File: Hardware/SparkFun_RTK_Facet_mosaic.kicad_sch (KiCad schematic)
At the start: 29 parts, among them J3 Qwiic_RA, J5 Conn_01x12_FPC_0.5mm, J6 Conn_01x12_FPC_0.5mm, J7 Conn_01x12_FPC_0.5mm, U1 ESP32-PICO-V3-02

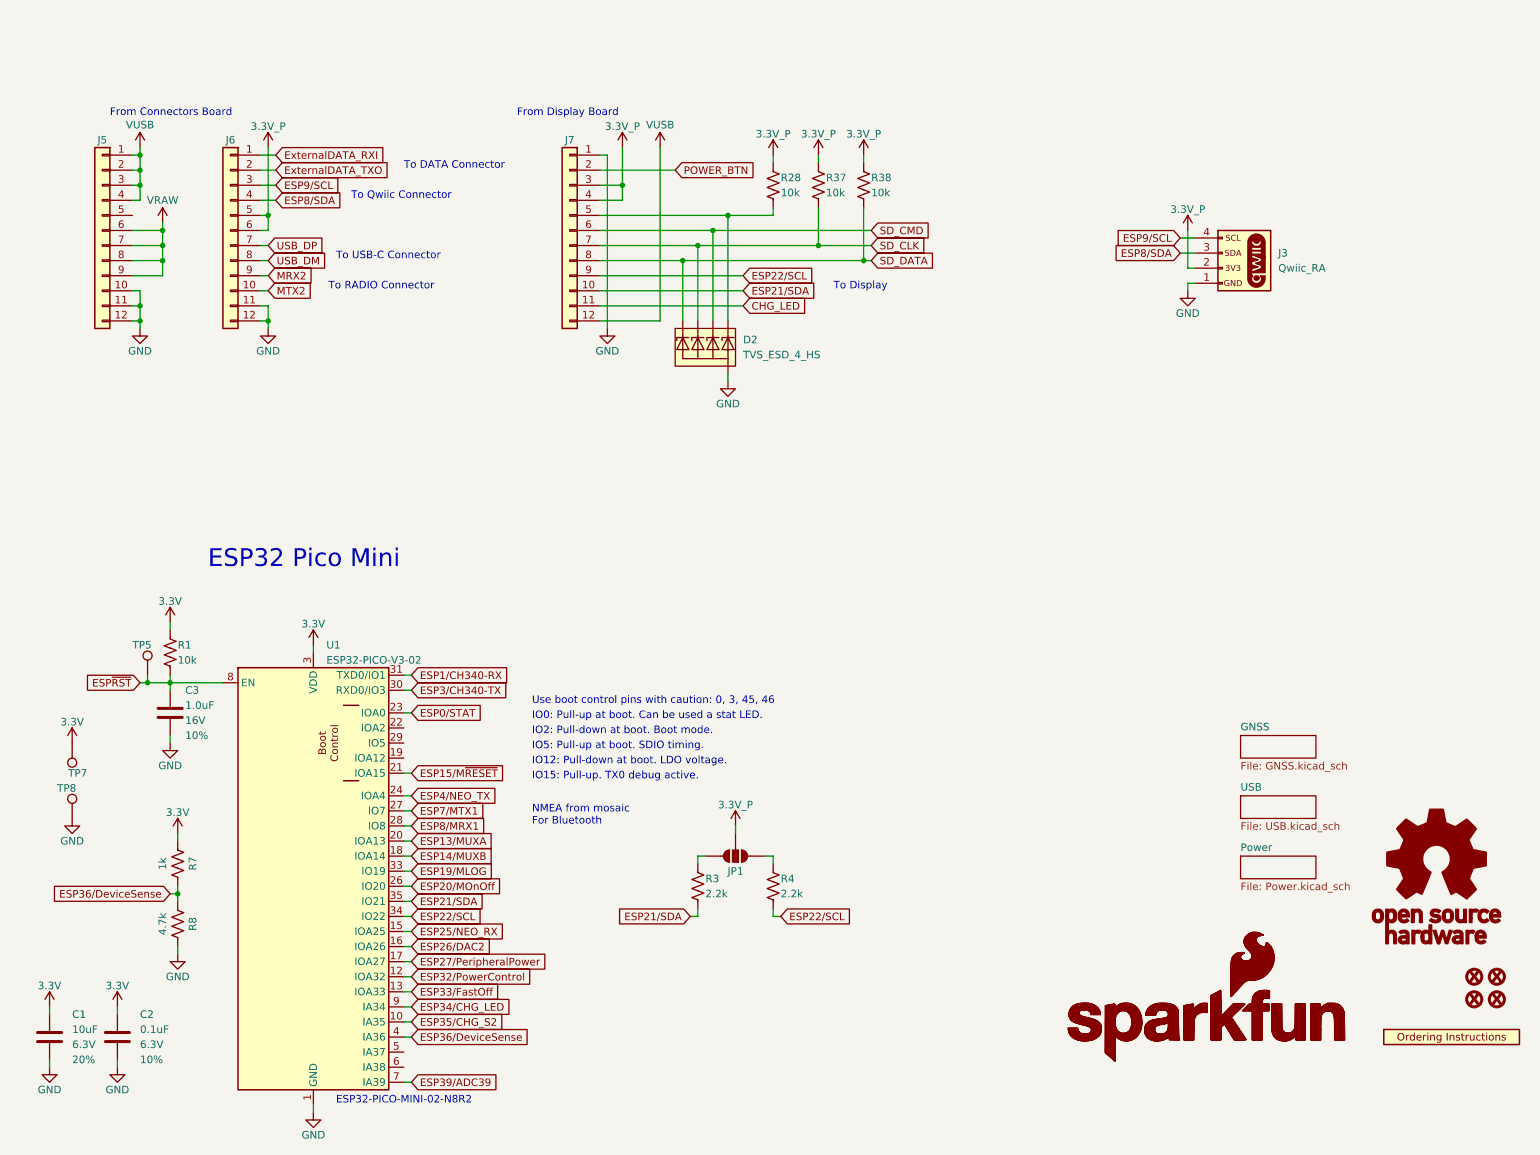
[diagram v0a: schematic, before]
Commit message: Schematic updates
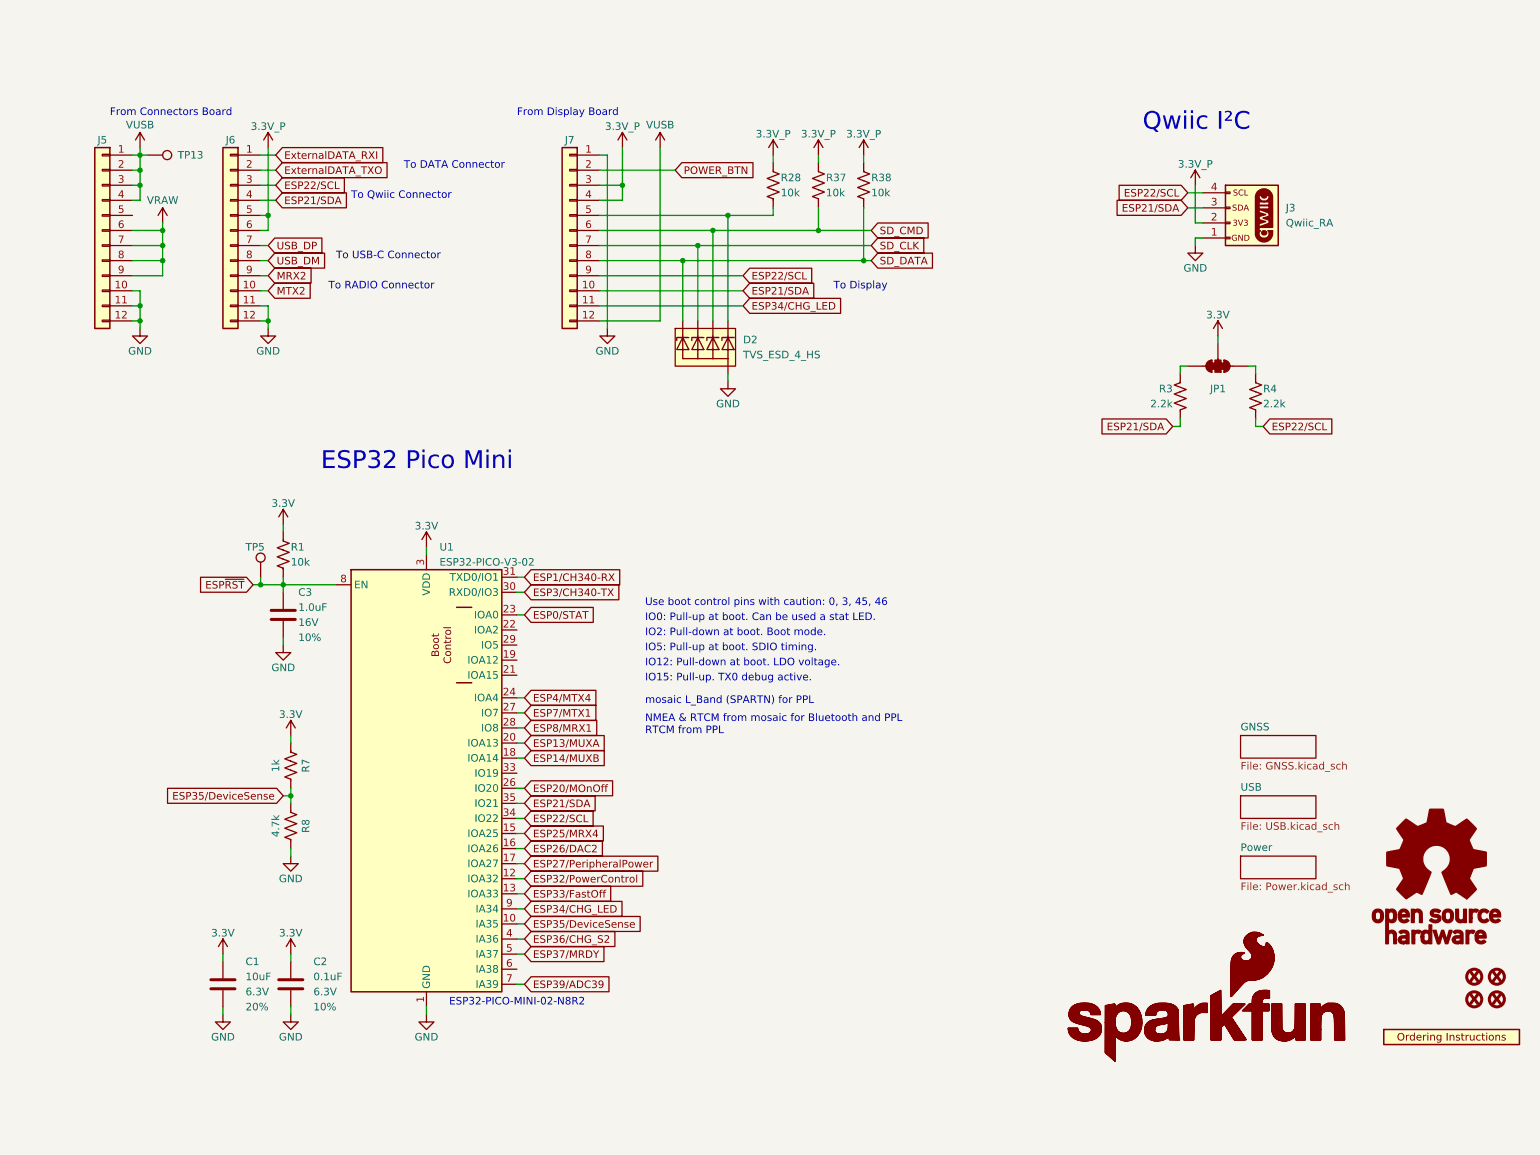
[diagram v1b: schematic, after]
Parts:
- removed JP1: ~, SparkFun-Jumper:SMT-JUMPER_3_NO_SILK, symbol SparkFun-Jumper:SolderJumper_3_Open
- removed TP7, TP8: PTH, SparkFun-Connector:1X01, symbol SparkFun-Connector:TestPoint_PTH
- added JP1: ~, SparkFun-Jumper:SMT-JUMPER_3_2-NC_TRACE_SILK, symbol SparkFun-Jumper:SolderJumper_3_Bridged123
- added TP13: PTH, SparkFun-Connector:1X01, symbol SparkFun-Connector:TestPoint_PTH
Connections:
- net CHG_LED is gone; now on net ESP34/CHG_LED: J7.11 (Pin_11)
- net ESP8/SDA is gone; now on net ESP21/SDA: J3.3 (Pin_3), J6.4 (Pin_4)
- net ESP9/SCL is gone; now on net ESP22/SCL: J3.4 (Pin_4), J6.3 (Pin_3)
- net 3.3V: now also JP1.2 (C)
- net SD_CLK: no longer R37.2
- net SD_CMD: now also R37.2
- net VUSB: now also TP13.1
- net at R4.1: now also JP1.1 (A)
- net at R3.1: now also JP1.3 (B)
- net ESP37/MRDY: now reaches U1.5 (IA37)
- net ESP15/M~{RESET}: no longer names the net of U1.21 (IOA15)
- net ESP19/MLOG: no longer names the net of U1.33 (IO19)
- net ESP25/NEO_RX renamed ESP25/MRX4
- net ESP35/CHG_S2 renamed ESP35/DeviceSense
- net ESP35/DeviceSense: now also R7.2, R8.1
- removed net ESP36/DeviceSense: R7.2, R8.1, U1.4 (IA36)
- net ESP4/NEO_TX renamed ESP4/MTX4
- new net ESP36/CHG_S2: U1.4 (IA36)
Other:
- note added: "NMEA & RTCM from mosaic for Bluetooth and PPL RTCM from PPL"
- note added: "Qwiic I²C"
- note added: "mosaic L_Band (SPARTN) for PPL"
- note removed: "NMEA from mosaic For Bluetooth"
- moved on the sheet: C1, C2, C3, J3, R1, R3, R4, R7, R8, TP5, U1

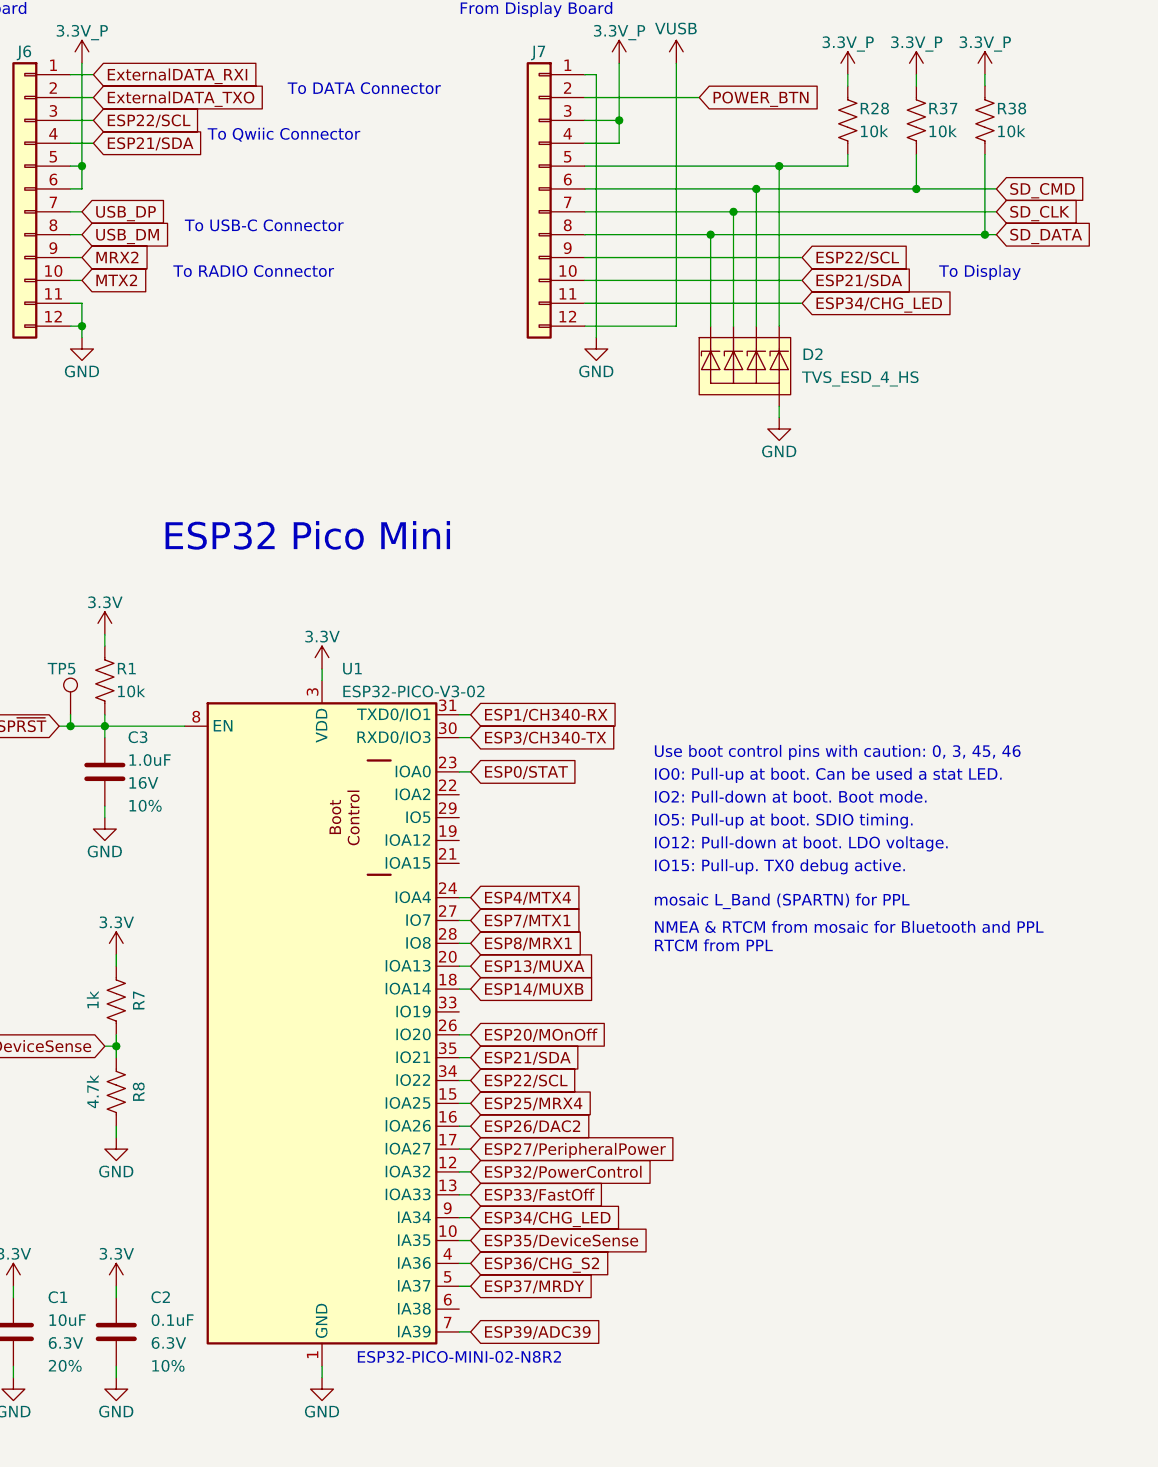
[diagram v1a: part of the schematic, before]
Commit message: Ready for airwire review
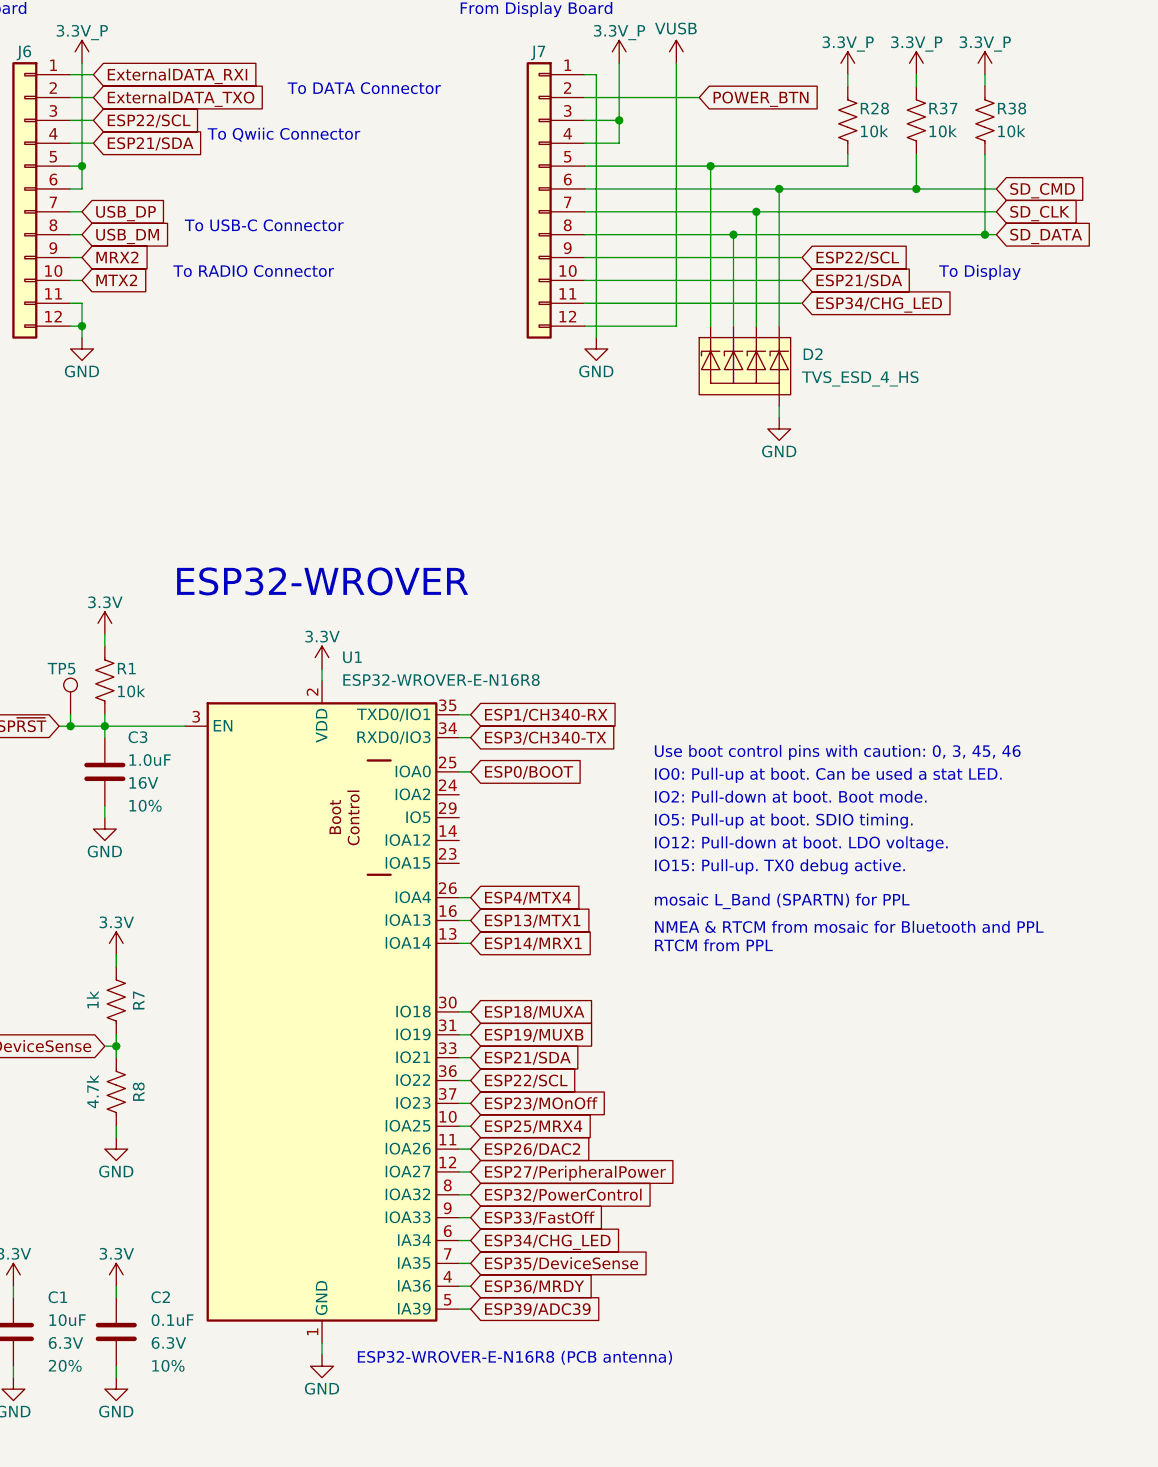
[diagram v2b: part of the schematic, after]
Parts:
- removed U1: ESP32-PICO-V3-02, SparkFun-RF:ESP32-PICO-MINI, symbol SparkFun-RF:ESP32-PICO-V3-02
- added U1: ESP32-WROVER-E-N16R8, SparkFun-RF:ESP32-WROVER-E-IE, symbol SparkFun-RF:ESP32-WROVER-E-N16R8
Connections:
- net 3.3V: now also U1.2 (VDD)
- net ESP1/CH340-RX: now also U1.35 (TXD0/IO1)
- net ESP21/SDA: now also U1.33 (IO21)
- net ESP22/SCL: now also U1.36 (IO22)
- net ESP25/MRX4: now also U1.10 (IOA25)
- net ESP26/DAC2: now also U1.11 (IOA26)
- net ESP27/PeripheralPower: now also U1.12 (IOA27)
- net ESP32/PowerControl: now also U1.8 (IOA32)
- net ESP33/FastOff: now also U1.9 (IOA33)
- net ESP34/CHG_LED: now also U1.6 (IA34)
- net ESP35/DeviceSense: now also U1.7 (IA35)
- net ESP39/ADC39: now also U1.5 (IA39)
- net ESP3/CH340-TX: now also U1.34 (RXD0/IO3)
- net ESP4/MTX4: now also U1.26 (IOA4)
- net ESP~{RST}: now also U1.3 (EN)
- net GND: now also U1.1 (GND), U1.15 (GND), U1.38 (GND), U1.39.1 (GND), U1.39.2 (GND), U1.39.3 (GND), U1.39.4 (GND), U1.39.5 (GND), U1.39.6 (GND), U1.39.7 (GND), U1.39.8 (GND), U1.39.9 (GND)
- net SD_CLK: now also D2.4 (K3); no longer D2.3 (K2)
- net SD_CMD: now also D2.5 (K4); no longer D2.4 (K3)
- net SD_DATA: now also D2.3 (K2); no longer D2.1 (K1)
- net at J7.5 (Pin_5), R28.2: now also D2.1 (K1); no longer D2.5 (K4)
- new net ESP0/BOOT: U1.25 (IOA0)
- new net ESP13/MTX1: U1.16 (IOA13)
- new net ESP14/MRX1: U1.13 (IOA14)
- new net ESP18/MUXA: U1.30 (IO18)
- new net ESP19/MUXB: U1.31 (IO19)
- new net ESP23/MOnOff: U1.37 (IO23)
- new net ESP36/MRDY: U1.4 (IA36)
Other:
- note added: "ESP32-WROVER"
- note added: "ESP32-WROVER-E-N16R8 (PCB antenna)"
- note removed: "ESP32 Pico Mini"
- note removed: "ESP32-PICO-MINI-02-N8R2"

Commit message: Work in progress...
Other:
- note added: "Use boot control pins with caution: 0, 2, 5, 12, 15"
- note removed: "Use boot control pins with caution: 0, 3, 45, 46"
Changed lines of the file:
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@@
     (effects (font (size 1.27 1.27)) (justify left bottom))
   )
-  (text "To Qwiic Connector" (at 69.85 44.45 0)
+  (text "To Qwiic Connector" (at 72.39 44.45 0)
     (effects (font (size 1.27 1.27)) (justify left bottom))
   )
@@
     (effects (font (size 1.27 1.27)) (justify left bottom))
   )
-  (text "Use boot control pins with caution: 0, 3, 45, 46" (at 119.38 113.03 0)
+  (text "Use boot control pins with caution: 0, 2, 5, 12, 15"
+    (at 119.38 113.03 0)
     (effects (font (size 1.27 1.27)) (justify left bottom))
   )
